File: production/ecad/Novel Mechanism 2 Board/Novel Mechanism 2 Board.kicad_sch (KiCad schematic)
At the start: 0 parts

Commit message: added driver ic to schematic
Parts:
- added U1: L9958SBTR, Package_SO:SOP80P1410X360-17N, symbol L9958SBTR:L9958SBTR
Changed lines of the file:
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@@
 (kicad_sch (version 20230121) (generator eeschema)
   (paper "A4")
+  (symbol (lib_id "L9958SBTR:L9958SBTR") (at 148.59 100.33 0) (unit 1)
+    (in_bom yes) (on_board yes) (dnp no) (fields_autoplaced)
+    (property "Reference" "U1" (at 148.59 69.85 0)
+      (effects (font (size 1.27 1.27)))
+    )
+    (property "Value" "L9958SBTR" (at 148.59 72.39 0)
+      (effects (font (size 1.27 1.27)))
+    )
+    (property "Footprint" "Package_SO:SOP80P1410X360-17N" (at 148.59 100.33 0)
+      (effects (font (size 1.27 1.27)) (justify bottom) hide)
+    )
+    (property "Datasheet" "" (at 148.59 100.33 0)
+      (effects (font (size 1.27 1.27)) hide)
+    )
+    (property "PARTREV" "6" (at 148.59 100.33 0)
+      (effects (font (size 1.27 1.27)) (justify bottom) hide)
+    )
+    (property "MF" "STMicroelectronics" (at 148.59 100.33 0)
+      (effects (font (size 1.27 1.27)) (justify bottom) hide)
+    )
+    (property "STANDARD" "IPC-7351B" (at 148.59 100.33 0)
+      (effects (font (size 1.27 1.27)) (justify bottom) hide)
+    )
+    (pin "12")
+    (pin "13")
+    (pin "9")
+    (pin "15")
+    (pin "16")
+    (pin "14")
+    (pin "8")
+    (pin "11")
+    (pin "5")
+    (pin "3")
+    (pin "10")
+    (pin "2")
+    (pin "1")
+    (pin "4")
+    (pin "7")
+    (pin "17")
+    (pin "6")
+    (instances
+      (project "Novel Mechanism 2 Board"
+        (path "/148ef552-79ac-46c4-a436-ee743f083e73"
+          (reference "U1") (unit 1)
+        )
+      )
+    )
+  )
   (sheet_instances
     (path "/" (page "1"))

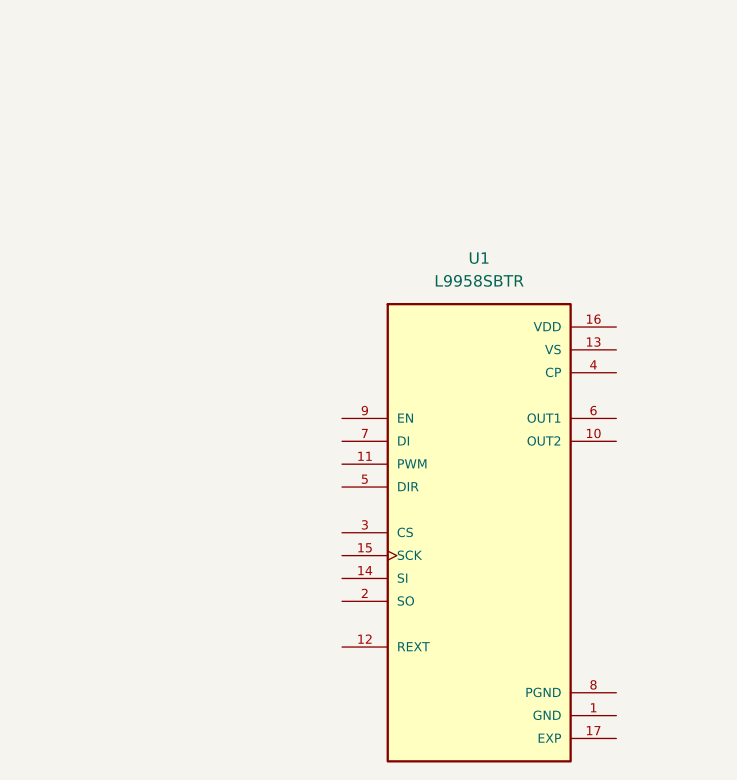
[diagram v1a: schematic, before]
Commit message: power port and zener added
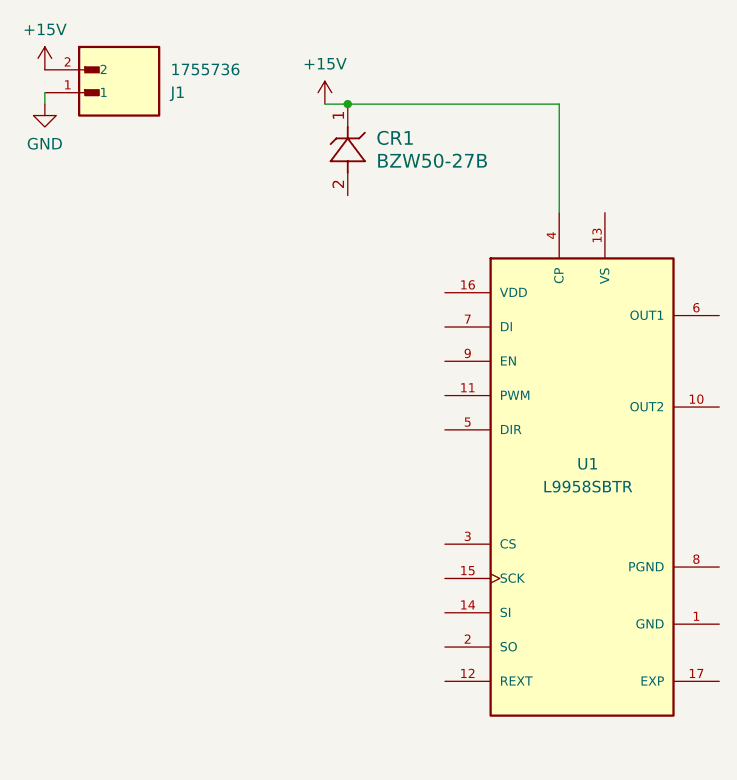
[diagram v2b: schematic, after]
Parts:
- added CR1: BZW50-27B, R6_STM, symbol BZW50-27B:BZW50-27B
- added J1: 1755736, 1755736:PHOENIX_1755736, symbol 1755736:1755736
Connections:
- net +15V: now reaches U1.4 (CP)
- net +15V: now also CR1.1, J1.2
- new net GND: J1.1
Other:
- moved on the sheet: U1
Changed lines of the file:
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@@
 (kicad_sch (version 20230121) (generator eeschema)
   (paper "A4")
-  (symbol (lib_id "L9958SBTR:L9958SBTR") (at 148.59 100.33 0) (unit 1)
-    (in_bom yes) (on_board yes) (dnp no) (fields_autoplaced)
-    (property "Reference" "U1" (at 148.59 69.85 0)
+  (junction (at 133.985 52.705) (diameter 0) (color 0 0 0 0)
+  )
+  (wire (pts (xy 131.445 52.705) (xy 133.985 52.705))
+    (stroke (width 0) (type default))
+  )
+  (wire (pts (xy 100.33 51.435) (xy 100.33 52.705))
+    (stroke (width 0) (type default))
+  )
+  (wire (pts (xy 133.985 52.705) (xy 157.48 52.705))
+    (stroke (width 0) (type default))
+  )
+  (wire (pts (xy 157.48 52.705) (xy 157.48 64.77))
+    (stroke (width 0) (type default))
+  )
+  (symbol (lib_id "L9958SBTR:L9958SBTR") (at 160.02 95.25 0) (unit 1)
+    (in_bom yes) (on_board yes) (dnp no)
+    (property "Reference" "U1" (at 160.655 92.71 0)
       (effects (font (size 1.27 1.27)))
     )
-    (property "Value" "L9958SBTR" (at 148.59 72.39 0)
+    (property "Value" "L9958SBTR" (at 160.655 95.25 0)
       (effects (font (size 1.27 1.27)))
     )
-    (property "Footprint" "Package_SO:SOP80P1410X360-17N" (at 148.59 100.33 0)
+    (property "Footprint" "Package_SO:SOP80P1410X360-17N" (at 160.02 95.25 0)
       (effects (font (size 1.27 1.27)) (justify bottom) hide)
     )
-    (property "Datasheet" "" (at 148.59 100.33 0)
+    (property "Datasheet" "" (at 160.02 95.25 0)
       (effects (font (size 1.27 1.27)) hide)
     )
-    (property "PARTREV" "6" (at 148.59 100.33 0)
+    (property "PARTREV" "6" (at 160.02 95.25 0)
       (effects (font (size 1.27 1.27)) (justify bottom) hide)
     )
-    (property "MF" "STMicroelectronics" (at 148.59 100.33 0)
+    (property "MF" "STMicroelectronics" (at 160.02 95.25 0)
       (effects (font (size 1.27 1.27)) (justify bottom) hide)
     )
-    (property "STANDARD" "IPC-7351B" (at 148.59 100.33 0)
+    (property "STANDARD" "IPC-7351B" (at 160.02 95.25 0)
       (effects (font (size 1.27 1.27)) (justify bottom) hide)
     )
@@
         )
       )
+    )
+  )
+  (symbol (lib_id "1755736:1755736") (at 107.95 51.435 0) (mirror x) (unit 1)
+    (in_bom yes) (on_board yes) (dnp no)
+    (property "Reference" "J1" (at 114.3 51.435 0)
+      (effects (font (size 1.27 1.27)) (justify left))
+    )
+    (property "Value" "1755736" (at 114.3 48.895 0)
+      (effects (font (size 1.27 1.27)) (justify left))
+    )
+    (property "Footprint" "1755736:PHOENIX_1755736" (at 107.95 51.435 0)
+      (effects (font (size 1.27 1.27)) (justify bottom) hide)
+    )
+    (property "Datasheet" "" (at 107.95 51.435 0)
+      (effects (font (size 1.27 1.27)) hide)
+    )
+    (property "PARTREV" "11.07.2018" (at 107.95 51.435 0)
+      (effects (font (size 1.27 1.27)) (justify bottom) hide)
+    )
+    (property "STANDARD" "Manufacturer Recommendations" (at 107.95 51.435 0)
+      (effects (font (size 1.27 1.27)) (justify bottom) hide)
+    )
+    (property "MAXIMUM_PACKAGE_HEIGHT" "12.15mm" (at 107.95 51.435 0)
+      (effects (font (size 1.27 1.27)) (justify bottom) hide)
+    )
+    (property "MANUFACTURER" "Phoenix Contact" (at 107.95 51.435 0)
+      (effects (font (size 1.27 1.27)) (justify bottom) hide)
+    )
+    (pin "1")
+    (pin "2")
+    (instances
+      (project "Novel Mechanism 2 Board"
+        (path "/148ef552-79ac-46c4-a436-ee743f083e73"
+          (reference "J1") (unit 1)
+        )
+      )
+    )
+  )
+  (symbol (lib_id "power:+15V") (at 131.445 52.705 0) (unit 1)
+    (in_bom yes) (on_board yes) (dnp no) (fields_autoplaced)
+    (property "Reference" "#PWR03" (at 131.445 56.515 0)
+      (effects (font (size 1.27 1.27)) hide)
+    )
+    (property "Value" "+15V" (at 131.445 48.26 0)
+      (effects (font (size 1.27 1.27)))
+    )
+    (property "Footprint" "" (at 131.445 52.705 0)
+      (effects (font (size 1.27 1.27)) hide)
+    )
+    (property "Datasheet" "" (at 131.445 52.705 0)
+      (effects (font (size 1.27 1.27)) hide)
+    )
+    (pin "1")
+    (instances
+      (project "Novel Mechanism 2 Board"
+        (path "/148ef552-79ac-46c4-a436-ee743f083e73"
+          (reference "#PWR03") (unit 1)
+        )
+      )
+    )
+  )
+  (symbol (lib_id "power:+15V") (at 100.33 48.895 0) (unit 1)
+    (in_bom yes) (on_board yes) (dnp no) (fields_autoplaced)
+    (property "Reference" "#PWR02" (at 100.33 52.705 0)
+      (effects (font (size 1.27 1.27)) hide)
+    )
+    (property "Value" "+15V" (at 100.33 44.45 0)
+      (effects (font (size 1.27 1.27)))
+    )
+    (property "Footprint" "" (at 100.33 48.895 0)
+      (effects (font (size 1.27 1.27)) hide)
+    )
+    (property "Datasheet" "" (at 100.33 48.895 0)
+      (effects (font (size 1.27 1.27)) hide)
+    )
+    (pin "1")
+    (instances
+      (project "Novel Mechanism 2 Board"
+        (path "/148ef552-79ac-46c4-a436-ee743f083e73"
+          (reference "#PWR02") (unit 1)
+        )
+      )
+    )
+  )
+  (symbol (lib_id "BZW50-27B:BZW50-27B") (at 133.985 52.705 270) (unit 1)
+    (in_bom yes) (on_board yes) (dnp no) (fields_autoplaced)
+    (property "Reference" "CR1" (at 137.16 56.515 90)
+      (effects (font (size 1.524 1.524)) (justify left))
+    )
+    (property "Value" "BZW50-27B" (at 137.16 59.055 90)
+      (effects (font (size 1.524 1.524)) (justify left))
+    )
+    (property "Footprint" "R6_STM" (at 133.985 52.705 0)
+      (effects (font (size 1.27 1.27) italic) hide)
+    )
+    (property "Datasheet" "BZW50-27B" (at 133.985 52.705 0)
+      (effects (font (size 1.27 1.27) italic) hide)
+    )
+    (pin "2")
+    (pin "1")
+    (instances
+      (project "Novel Mechanism 2 Board"
+        (path "/148ef552-79ac-46c4-a436-ee743f083e73"
+          (reference "CR1") (unit 1)
+        )
+      )
+    )
+  )
+  (symbol (lib_id "power:GND") (at 100.33 52.705 0) (unit 1)
+    (in_bom yes) (on_board yes) (dnp no) (fields_autoplaced)
+    (property "Reference" "#PWR01" (at 100.33 59.055 0)
+      (effects (font (size 1.27 1.27)) hide)
+    )
+    (property "Value" "GND" (at 100.33 57.15 0)
+      (effects (font (size 1.27 1.27)))
+    )
+    (property "Footprint" "" (at 100.33 52.705 0)
+      (effects (font (size 1.27 1.27)) hide)
+    )
+    (property "Datasheet" "" (at 100.33 52.705 0)
+      (effects (font (size 1.27 1.27)) hide)
+    )
+    (pin "1")
+    (instances
+      (project "Novel Mechanism 2 Board"
+        (path "/148ef552-79ac-46c4-a436-ee743f083e73"
+          (reference "#PWR01") (unit 1)
+        )
+      )

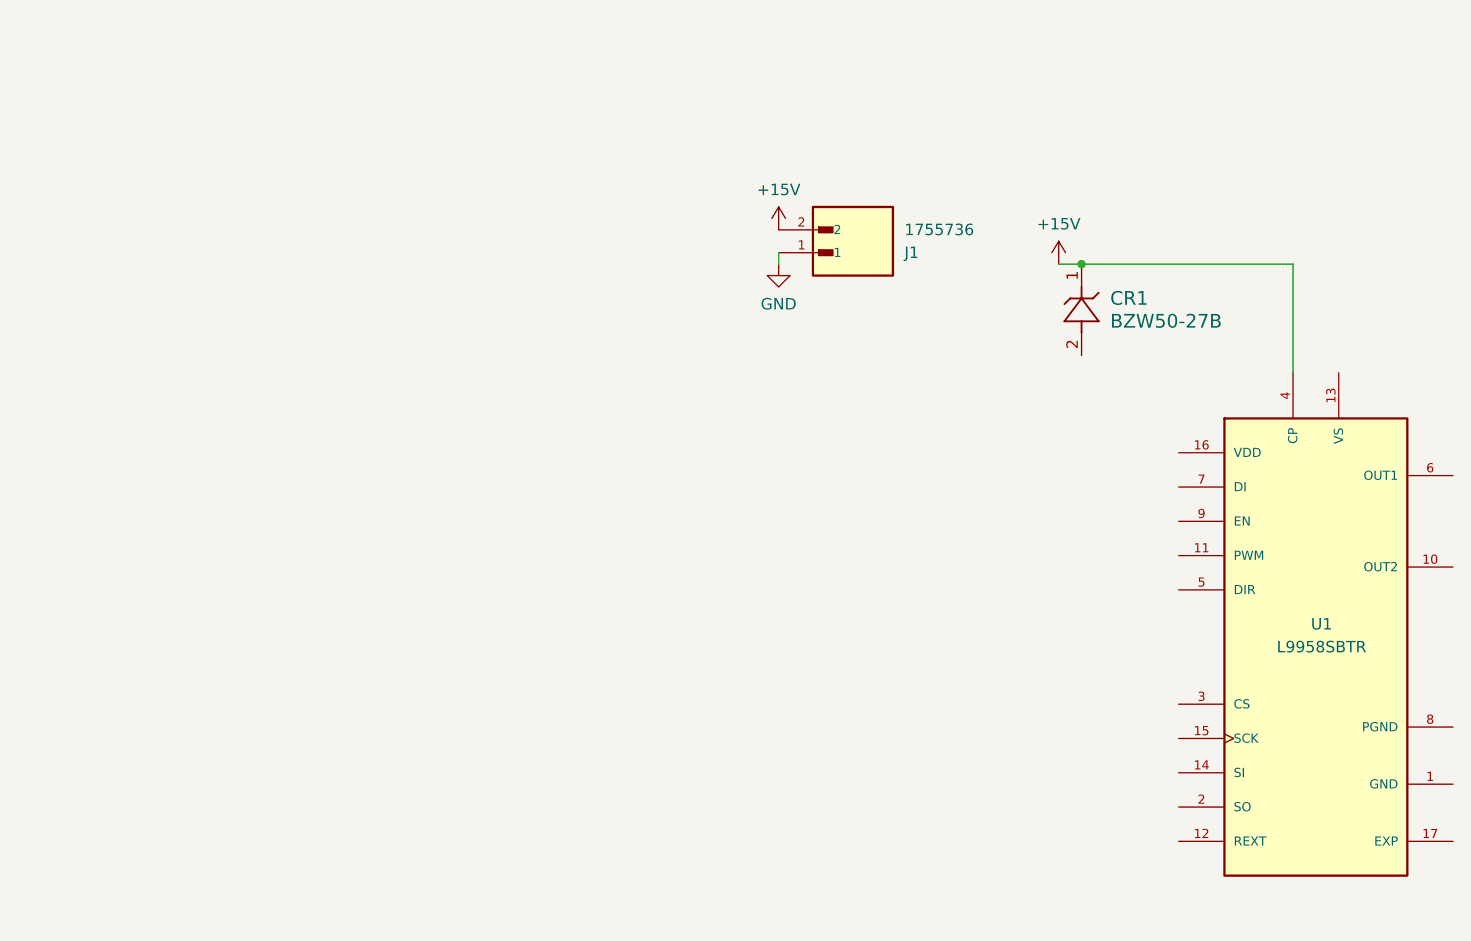
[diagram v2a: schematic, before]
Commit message: draft complete, need to test variable speed trigger before adding to schematic
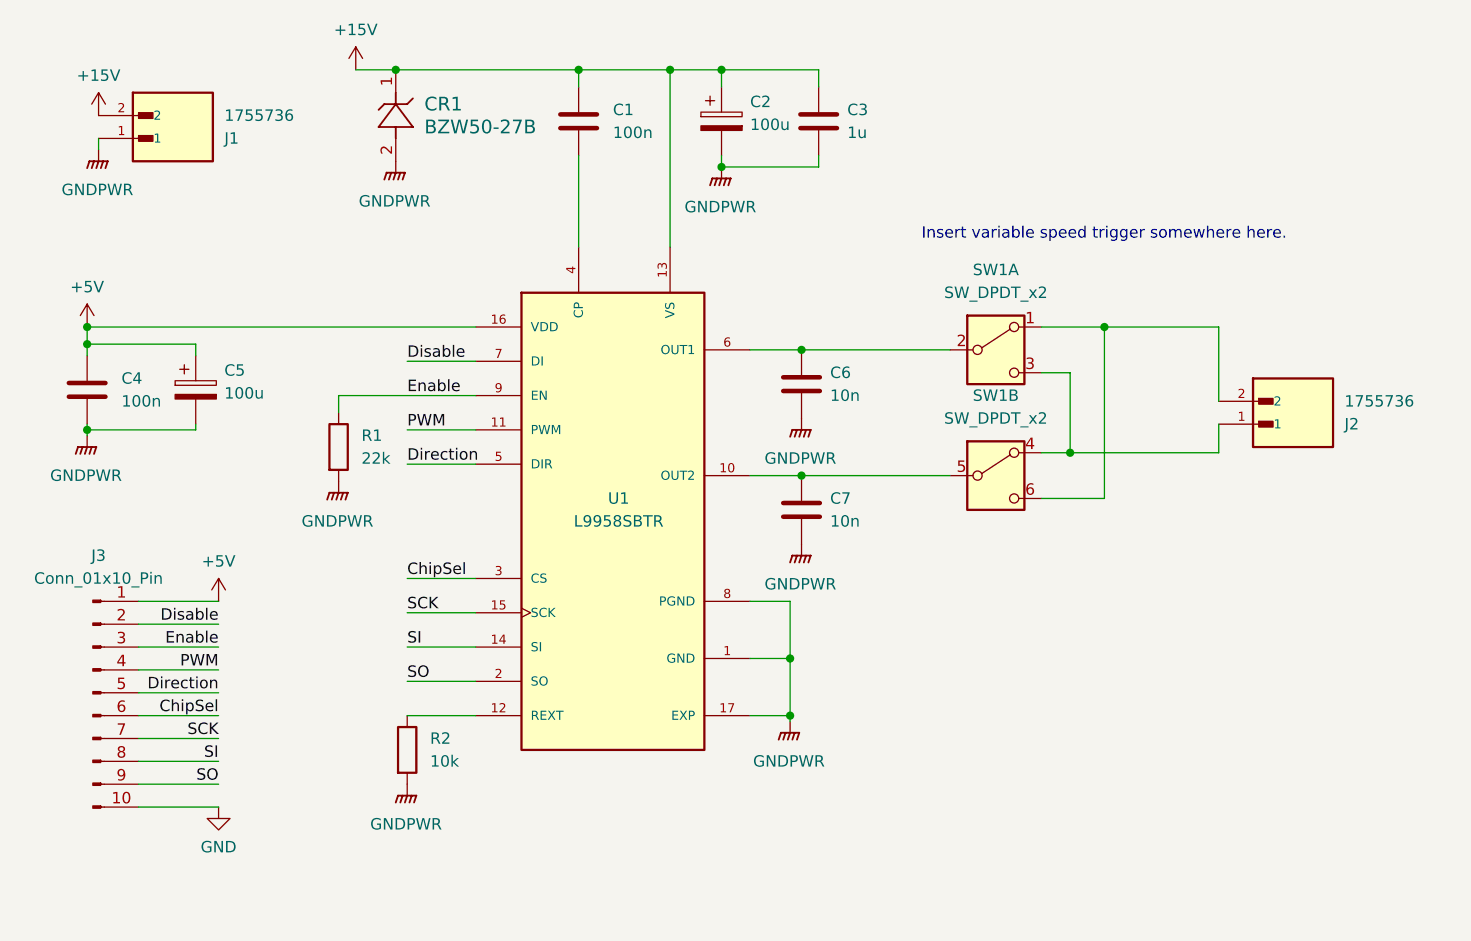
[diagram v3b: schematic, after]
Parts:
- added C1, C4: 100n, symbol Device:C
- added C2, C5: 100u, symbol Device:C_Polarized
- added C3: 1u, symbol Device:C
- added C6, C7: 10n, symbol Device:C
- added J2: 1755736, 1755736:PHOENIX_1755736, symbol 1755736:1755736
- added J3: Conn_01x10_Pin, symbol Connector:Conn_01x10_Pin
- added R1: 22k, symbol Device:R
- added R2: 10k, symbol Device:R
- added SW1: SW_DPDT_x2, symbol Switch:SW_DPDT_x2
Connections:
- net +15V: now also U1.13 (VS), C1.1, C2.1, C3.1; no longer U1.4 (CP)
- net GND: now also J3.10 (Pin_10); no longer J1.1
- net GNDPWR: now reaches U1.1 (GND)
- net GNDPWR: now also CR1.2, J1.1, U1.17 (EXP), U1.8 (PGND), C2.2, C3.2, C4.2, C5.2, C6.2, C7.2, R1.2, R2.2
- net at U1.10 (OUT2): now also C7.1, SW1.5 (B)
- net PWM: now reaches U1.11 (PWM)
- net PWM: now also J3.4 (Pin_4)
- net at U1.12 (REXT): now also R2.1
- net SI: now reaches U1.14 (SI)
- net SI: now also J3.8 (Pin_8)
- net SCK: now reaches U1.15 (SCK)
- net SCK: now also J3.7 (Pin_7)
- net +5V: now reaches U1.16 (VDD)
- net +5V: now also C4.1, C5.1, J3.1 (Pin_1)
- net SO: now reaches U1.2 (SO)
- net SO: now also J3.9 (Pin_9)
- net ChipSel: now reaches U1.3 (CS)
- net ChipSel: now also J3.6 (Pin_6)
- net Direction: now reaches U1.5 (DIR)
- net Direction: now also J3.5 (Pin_5)
- net at U1.6 (OUT1): now also C6.1, SW1.2 (B)
- net Disable: now reaches U1.7 (DI)
- net Disable: now also J3.2 (Pin_2)
- net Enable: now reaches U1.9 (EN)
- net Enable: now also J3.3 (Pin_3), R1.1
- new net: C1.2, U1.4 (CP)
- new net: J2.1, SW1.3 (C), SW1.4 (A)
- new net: J2.2, SW1.1 (A), SW1.6 (C)
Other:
- note added: "Insert variable speed trigger somewhere here."
- moved on the sheet: CR1, J1, U1
